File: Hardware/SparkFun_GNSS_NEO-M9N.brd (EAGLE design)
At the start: 64.9 x 38 mm, 69 parts, among them J1 MICROMOD_STANDARD, U1 U-BLOX_NEO-M9N, U2 3.3V, U3 EEPROM, U4 74HC1G04

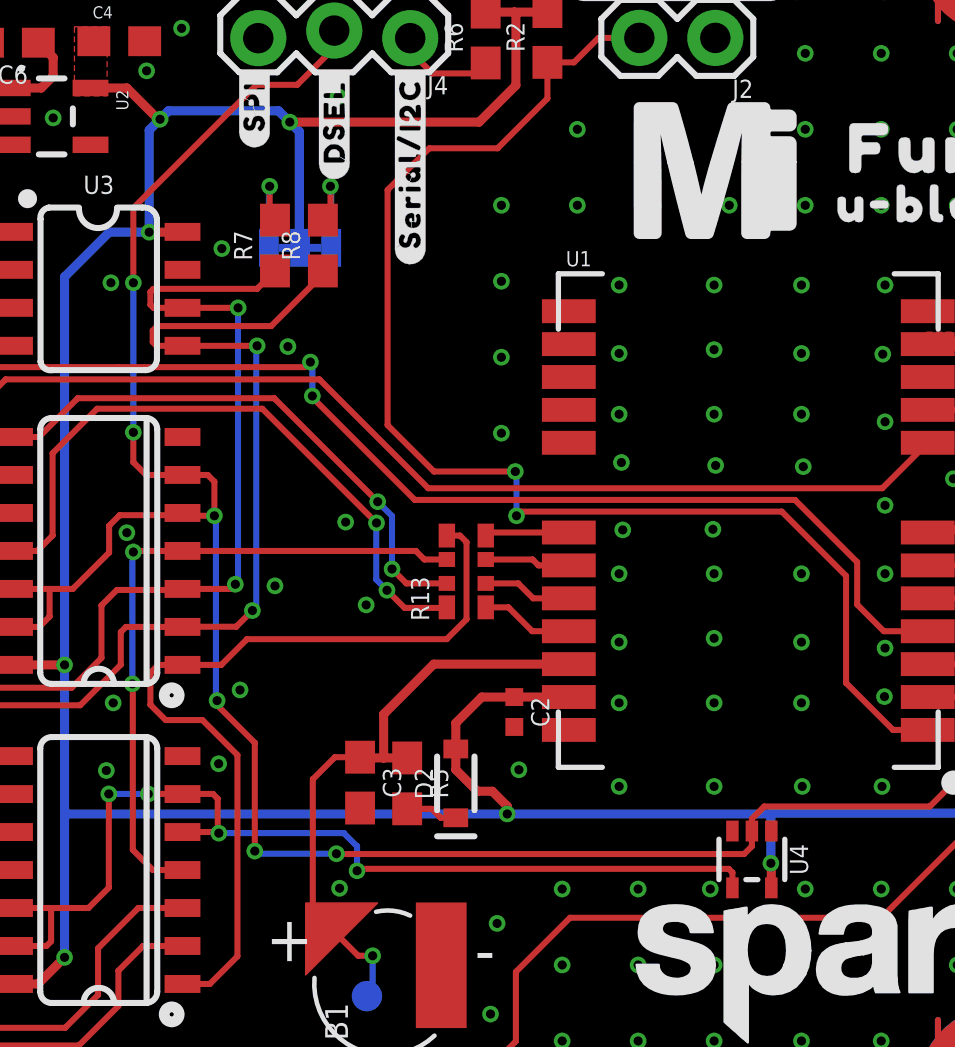
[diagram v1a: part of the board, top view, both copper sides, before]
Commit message: Loosely adds placement of WP circuit to PCB
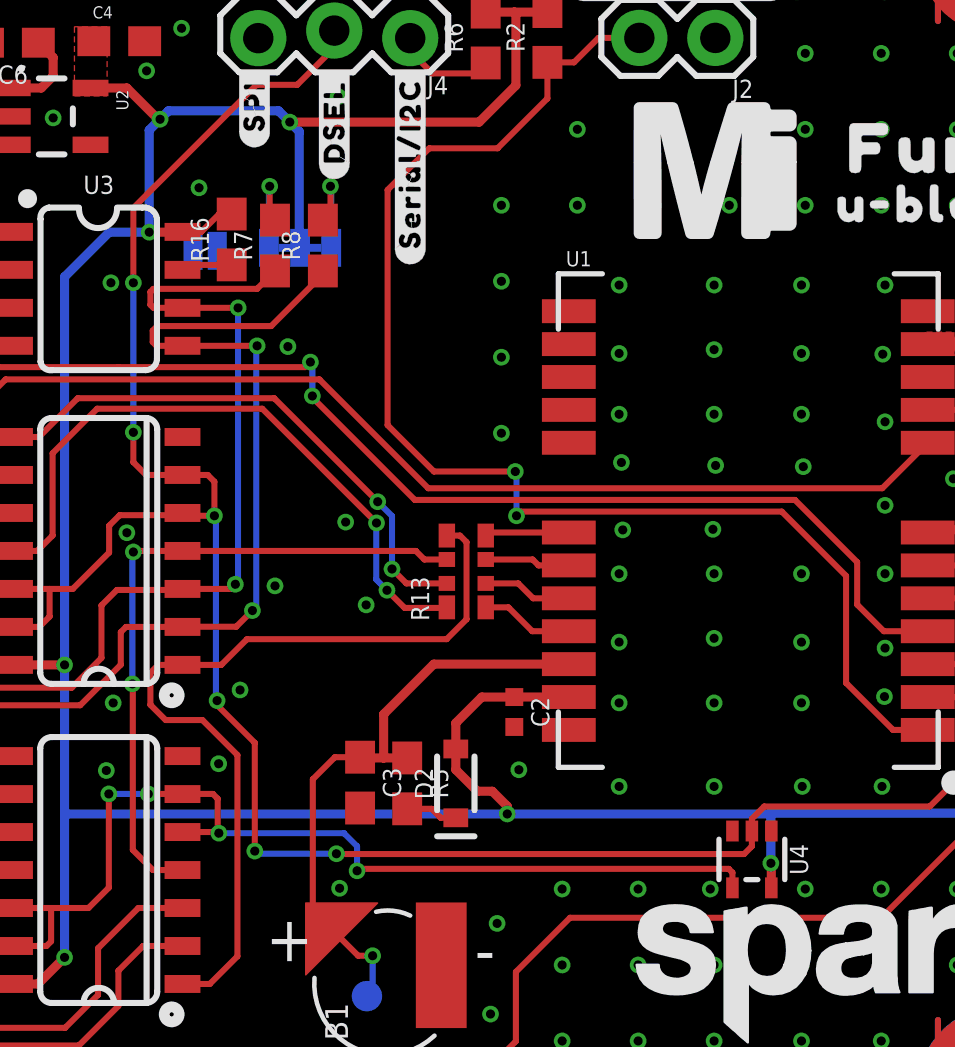
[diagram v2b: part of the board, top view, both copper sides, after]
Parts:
- added JP1: JUMPER-SMT_2_NO_SILK, SparkFun-Jumpers:SMT-JUMPER_2_NO_SILK
- added R16: 10k, SparkFun-Resistors:0603
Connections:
- new net WP: J1.40, JP1.2, R16.1, U3.7
- net 3.3V: now also R16.2
- net GND: now also JP1.1; no longer U3.7
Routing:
- net 3.3V: track 141.0 -> 142.9 mm
- net WP: track 0.00 -> 1.71 mm

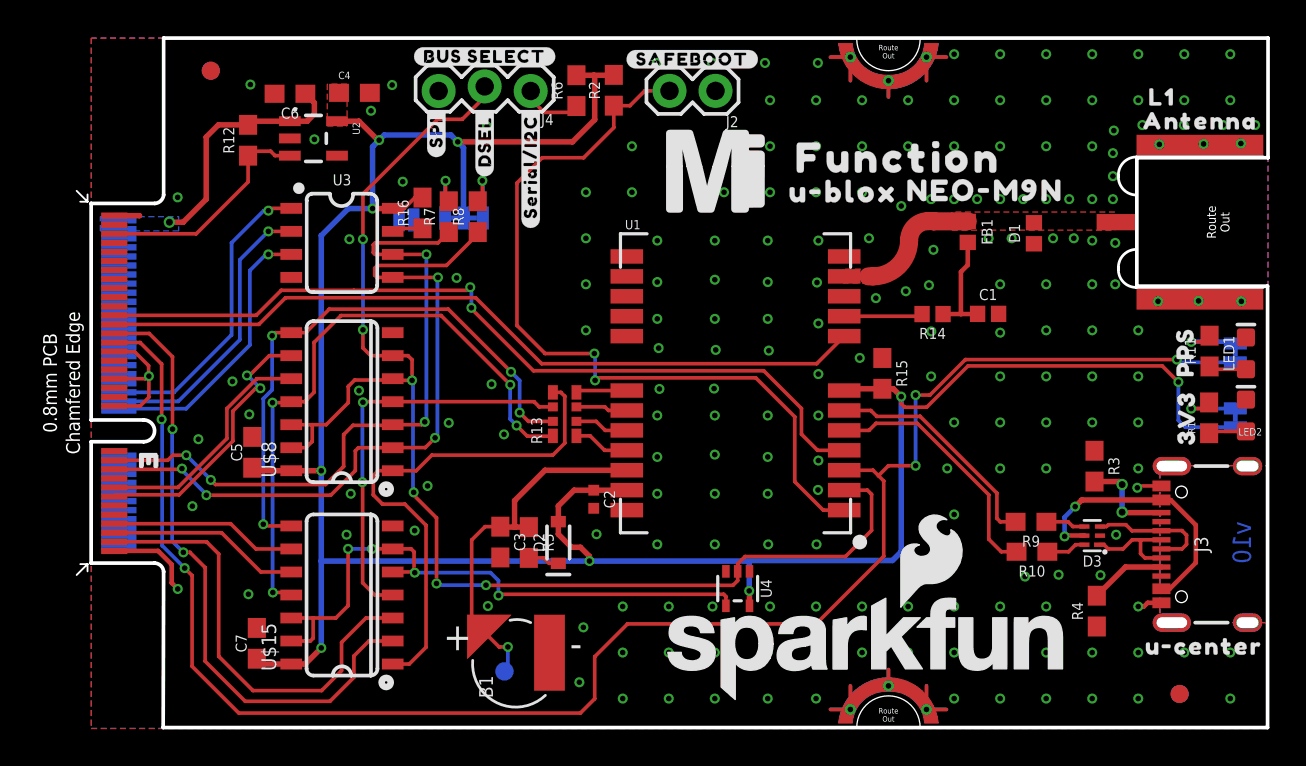
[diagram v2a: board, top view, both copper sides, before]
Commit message: Adds WP pullup resistor and jumper to allow user control over the pin
* Routes WP net to card's edge
* Adds silk to WP jumper
* Adjusts a few traces
* Rolls version to v11
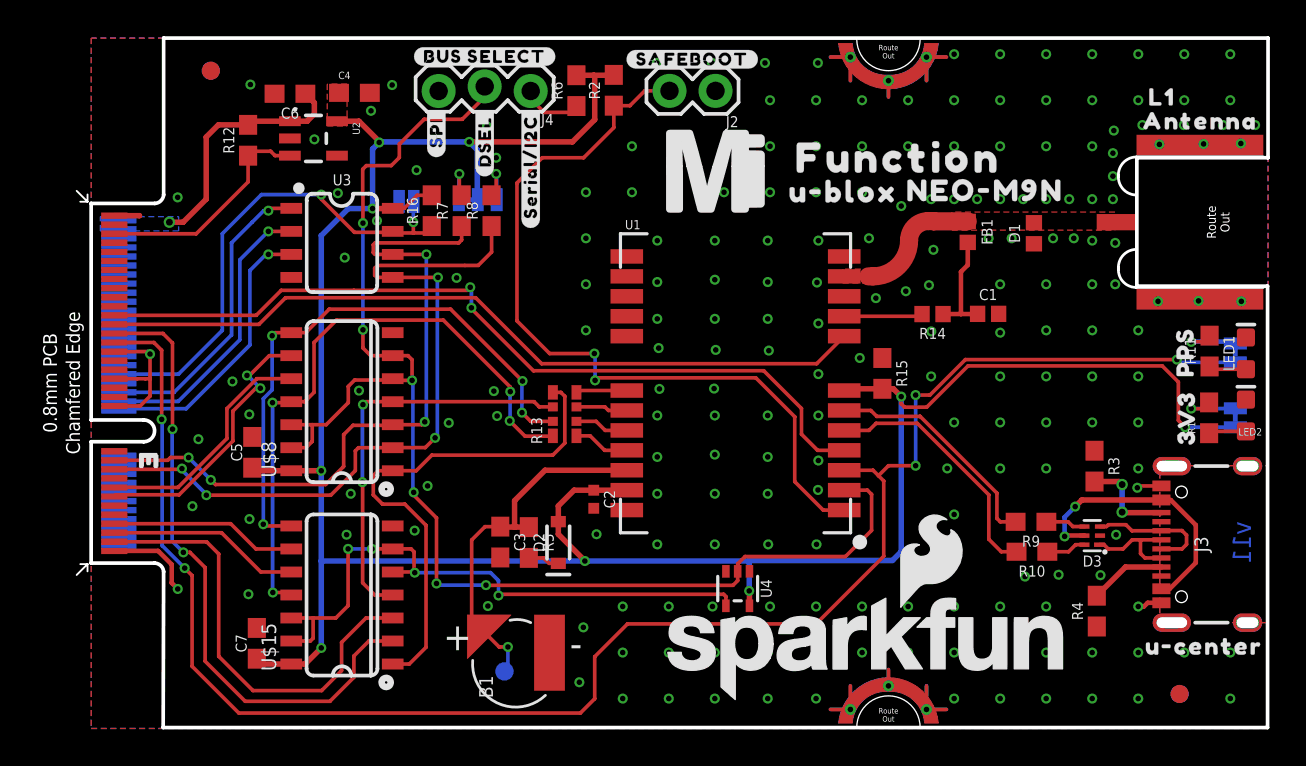
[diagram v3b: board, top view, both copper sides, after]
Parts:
- removed JP1: JUMPER-SMT_2_NO_SILK, SparkFun-Jumpers:SMT-JUMPER_2_NO_SILK
- added U$20: (no value), top:#WP#13215403132222564
- added WP: JUMPER-SMT_2_NO_SILK, SparkFun-Jumpers:SMT-JUMPER_2_NO_SILK
- J4: value (none) -> Bus Selection
- moved U$10 2.62 mm to (21.2, 27.4)
- moved JP5 1.27 mm to (21.3, 29.2)
- moved R8 0.83 mm to (22.1, 28.6)
- moved R7 0.78 mm to (20.4, 28.6)
- moved R16 0.52 mm to (18.8, 28.6)
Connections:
- net GND: now also WP.1; no longer JP1.1
- net WP: now also WP.2; no longer JP1.2
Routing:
- net WP: track 1.71 -> 27.5 mm, vias 0 -> 2
- net SDA: track 39.8 -> 41.4 mm
- net D_SEL: track 73.9 -> 75.1 mm
- net 3.3V: track 142.9 -> 141.8 mm
- net SCL: track 37.6 -> 38.7 mm
- net N$8: track 3.27 -> 2.67 mm
- net N$5: track 3.30 -> 2.72 mm
- net GND: track 22.4 -> 22.9 mm, vias 207 -> 211
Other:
- board text added: "v11"
- board text removed: "v10"

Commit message: Add 0.1uF bypass cap to EEPROM VCC, moves two PTH header east to accommodate new cap
* Adds "GNSS" silk
* Flips silk on bottom so that all silk has uniform direction
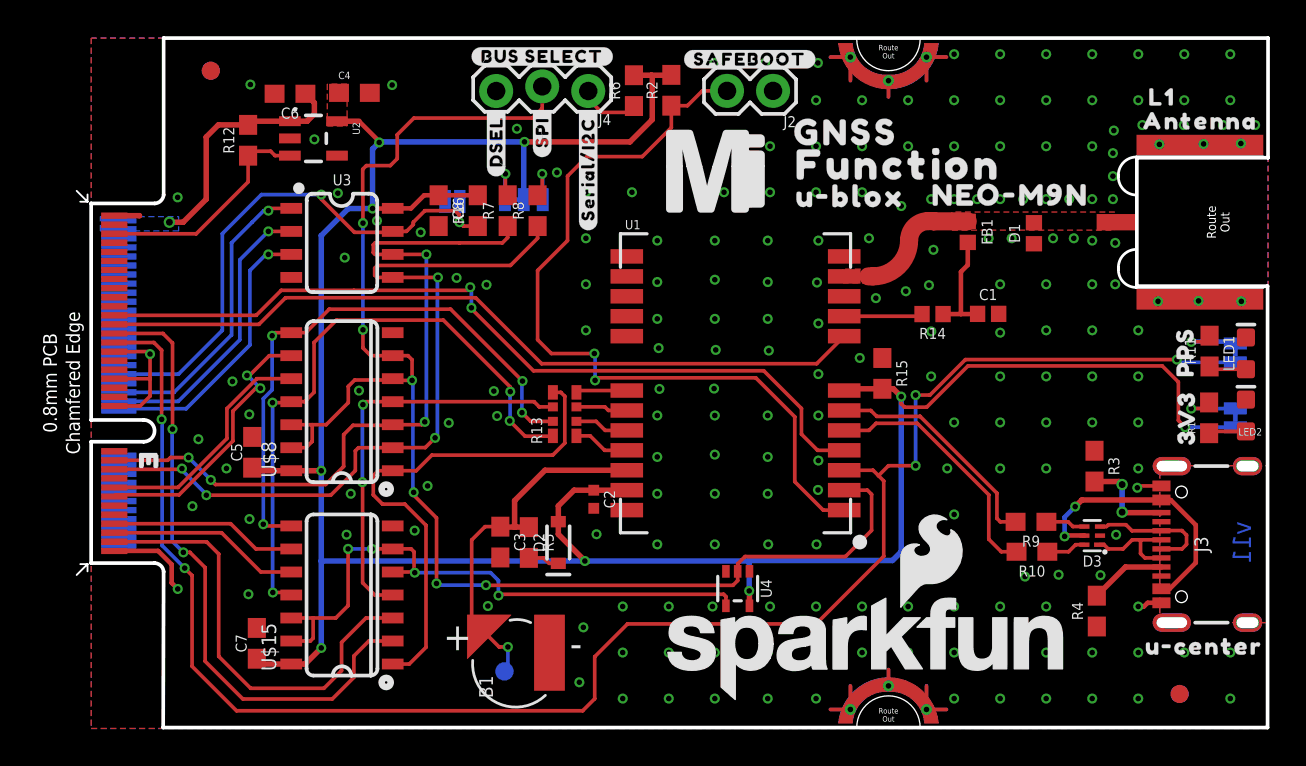
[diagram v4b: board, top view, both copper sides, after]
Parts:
- added C8: 0.1uF, SparkFun-Capacitors:0603
- added U$21: (no value), top:GNSS2222502
- U$12: device top:#3V3_LED#17 -> top:#3V3_LED#403132222514
- U$13: device top:#PPS_LED#17 -> top:#PPS_LED#403132222514
- moved U$16 5.84 mm to (24.9, 32.9)
- moved U$17 3.18 mm to (27.4, 30.9)
- moved U$18 3.18 mm to (24.9, 37.1)
- moved J2 3.17 mm to (37.6, 35.2)
- moved J4 3.17 mm to (27.4, 35.3)
- moved R2 3.17 mm to (32.0, 35.2)
- moved R6 3.17 mm to (30.0, 35.2)
- moved U$4 3.17 mm to (36.3, 36.9)
- moved U$10 2.67 mm to (23.9, 27.4)
- moved JP5 2.54 mm to (23.9, 29.2)
- moved R8 2.54 mm to (24.6, 28.6)
- moved R16 2.54 mm to (21.3, 28.6)
- moved R7 2.54 mm to (23.0, 28.6)
- moved WP 2.54 mm to (19.9, 29.1)
- moved U$20 2.41 mm to (19.8, 27.4)
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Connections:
- net 3.3V: now also C8.1
- net GND: now also C8.2
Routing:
- net 3.3V: track 141.8 -> 147.3 mm
- net D_SEL: track 75.1 -> 79.0 mm
- net WP: track 27.5 -> 30.4 mm
- net SCL: track 38.7 -> 41.2 mm
- net SDA: track 41.4 -> 43.5 mm
- net !SAFE: track 44.3 -> 45.0 mm
- net GND: vias 211 -> 209

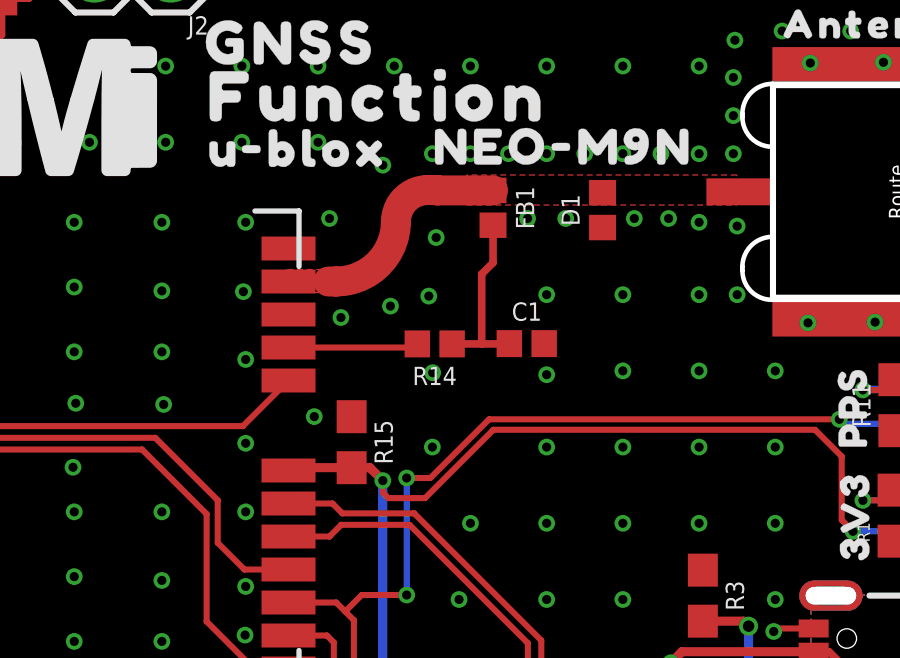
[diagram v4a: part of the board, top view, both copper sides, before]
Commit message: Updates Function Board symbol
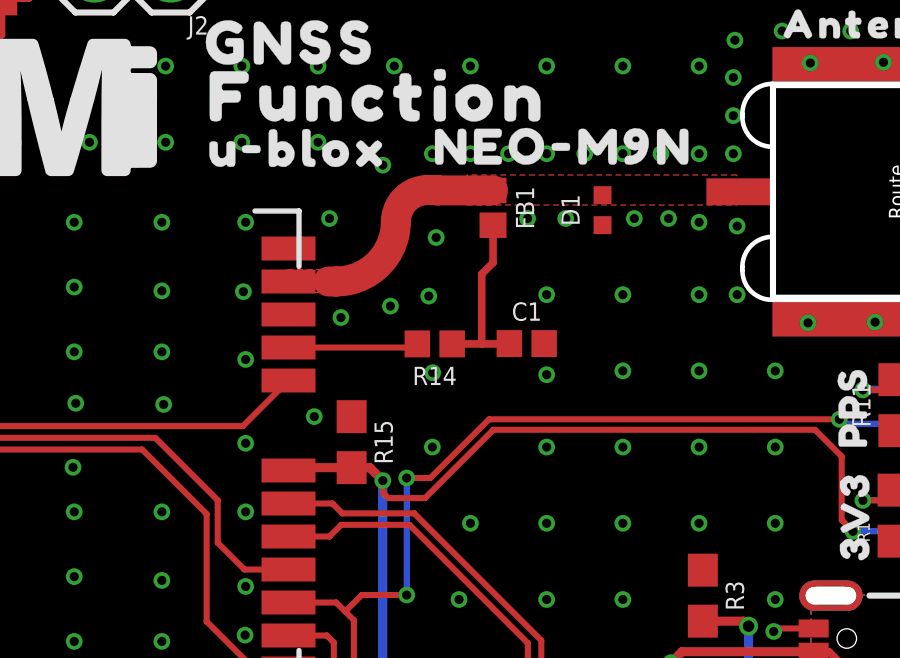
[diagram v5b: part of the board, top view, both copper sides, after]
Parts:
- D1: value PESD0402 -> PESD0402-0402T; device SparkFun-DiscreteSemi:0402 -> SparkFun-DiscreteSemi:0402-TIGHT
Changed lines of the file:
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@@
 <layer number="115" name="ReferenceISLANDS" color="7" fill="1" visible="no" active="no"/>
 <layer number="116" name="Patch_BOT" color="9" fill="4" visible="no" active="no"/>
-<layer number="117" name="PM_Ref" color="26" fill="1" visible="no" active="yes"/>
+<layer number="117" name="PM_Ref" color="26" fill="1" visible="yes" active="yes"/>
 <layer number="118" name="Rect_Pads" color="7" fill="1" visible="no" active="no"/>
-<layer number="119" name="PF_Ref" color="31" fill="1" visible="no" active="yes"/>
-<layer number="120" name="WFL_Ref" color="25" fill="1" visible="no" active="yes"/>
+<layer number="119" name="PF_Ref" color="31" fill="1" visible="yes" active="yes"/>
+<layer number="120" name="WFL_Ref" color="25" fill="1" visible="yes" active="yes"/>
 <layer number="121" name="_tsilk" color="7" fill="1" visible="no" active="no"/>
 <layer number="122" name="_bsilk" color="7" fill="1" visible="no" active="no"/>
@@
 <attribute name="VALUE" x="13.843" y="22.987" size="0.6096" layer="27" font="vector" ratio="20" align="bottom-center"/>
 </element>
-<element name="D1" library="SparkFun-DiscreteSemi" package="0402" value="PESD0402" x="52.0282" y="27.3288" smashed="yes" rot="R90">
-<attribute name="DIGIKEY_PART" value="PESD0402-140CT-ND" x="52.0282" y="27.3288" size="1.778" layer="27" font="vector" ratio="15" rot="R90" display="off"/>
-<attribute name="MOUSE_PART" value="650-PESD0402-140" x="52.0282" y="27.3288" size="1.778" layer="27" font="vector" ratio="15" rot="R90" display="off"/>
+<element name="D1" library="SparkFun-DiscreteSemi" package="0402-TIGHT" value="PESD0402-0402T" x="52.0282" y="27.3288" smashed="yes" rot="R90">
 <attribute name="NAME" x="51.2662" y="27.3288" size="0.6096" layer="25" font="vector" ratio="20" rot="R90" align="bottom-center"/>
 <attribute name="PROD_ID" value="DIO-15359" x="52.0282" y="27.3288" size="1.778" layer="27" font="vector" ratio="15" rot="R90" display="off"/>
@@
 <wire x1="27.7368" y1="13.1492" x2="27.7376" y2="13.15" width="0.3048" layer="1"/>
 <wire x1="27.7376" y1="13.15" x2="29.56" y2="13.15" width="0.3048" layer="1"/>
-<wire x1="41.668" y1="18.542" x2="41.56" y2="18.65" width="0.3048" layer="1"/>
 <wire x1="41.56" y1="18.65" x2="41.655" y2="18.745" width="0.3048" layer="1"/>
 <wire x1="41.655" y1="18.745" x2="43.6638" y2="18.745" width="0.3048" layer="1"/>
